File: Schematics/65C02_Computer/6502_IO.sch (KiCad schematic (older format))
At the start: 28 parts, among them J10 LCD Connector, J2 Optional UART Port, J3 USB_B_Micro, J4 USB_B, J5 Power Connector, J6 Mini-DIN-6, J8 VIA2PA, J9 VIA2PB, U10 ATtiny4313-PU, U11 65C22S, U12 65C22S, U5 65C51N, U6 FT230XS, X2 1.8432MHz

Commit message: Added ferrite bead, got rid of DRC errors, other changes
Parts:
- added FB1: Ferrite_Bead_Small, Resistor_THT:R_Axial_DIN0207_L6.3mm_D2.5mm_P7.62mm_Horizontal, symbol Device:Ferrite_Bead_Small
- J4: symbol Connector:USB_B -> 6502:USB_B
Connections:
- net +5V: now also FB1.1; no longer J3.1 (VBUS), J4.1 (VBUS)
- new net: FB1.2, J3.1 (VBUS), J4.1 (VBUS)
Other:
- moved on the sheet: J4
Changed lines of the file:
@@
 	2950 6800 2850 6800
 $Comp
-L Connector:USB_B J4
+L 6502:USB_B J4
 U 1 1 5E5D8CF6
-P 3950 6800
-F 0 "J4" H 4007 7267 50  0000 C CNN
-F 1 "USB_B" H 4007 7176 50  0000 C CNN
-F 2 "Connector_USB:USB_B_OST_USB-B1HSxx_Horizontal" H 4100 6750 50  0001 C CNN
-F 3 " ~" H 4100 6750 50  0001 C CNN
-	1    3950 6800
+P 4200 6800
+F 0 "J4" H 4257 7267 50  0000 C CNN
+F 1 "USB_B" H 4257 7176 50  0000 C CNN
+F 2 "Connector_USB:USB_B_OST_USB-B1HSxx_Horizontal" H 4350 6750 50  0001 C CNN
+F 3 " ~" H 4350 6750 50  0001 C CNN
+	1    4200 6800
 	1    0    0    -1
 $EndComp
-Text GLabel 3950 7300 3    50   Input ~ 0
+Text GLabel 4200 7300 3    50   Input ~ 0
 GND
-Text GLabel 4350 6600 2    50   Input ~ 0
-+5V
-Text GLabel 4350 6800 2    50   BiDi ~ 0
+Text GLabel 4600 6800 2    50   BiDi ~ 0
 PUSBD+
-Text GLabel 4350 6900 2    50   BiDi ~ 0
+Text GLabel 4600 6900 2    50   BiDi ~ 0
 PUSBD-
-NoConn ~ 3850 7200
+NoConn ~ 4100 7200
 Wire Wire Line
-	3950 7300 3950 7200
+	4200 7300 4200 7200
 Wire Wire Line
-	4250 6900 4350 6900
+	4500 6900 4600 6900
 Wire Wire Line
-	4250 6800 4350 6800
+	4500 6800 4600 6800
 Wire Wire Line
-	4250 6600 4350 6600
+	4500 6600 4600 6600
 Wire Wire Line
 	4000 2100 4000 2200
@@
 	2000 1450 1550 1450
 Connection ~ 1550 1450
-Text GLabel 5700 6600 2    50   Input ~ 0
+Text GLabel 6550 6600 2    50   Input ~ 0
 +5V
 Text GLabel 5300 7300 3    50   Input ~ 0
@@
 Text GLabel 1450 1450 0    50   BiDi ~ 0
 PUSBD-
+$Comp
+L Device:Ferrite_Bead_Small FB1
+U 1 1 5E6E4D6F
+P 6100 6600
+F 0 "FB1" V 5863 6600 50  0000 C CNN
+F 1 "Ferrite_Bead_Small" V 5954 6600 50  0000 C CNN
+F 2 "Resistor_THT:R_Axial_DIN0207_L6.3mm_D2.5mm_P7.62mm_Horizontal" V 6030 6600 50  0001 C CNN
+F 3 "~" H 6100 6600 50  0001 C CNN
+	1    6100 6600
+	0    1    1    0
+$EndComp
+Wire Wire Line
+	6200 6600 6400 6600
+Wire Wire Line
+	4600 6600 4600 6250
+Wire Wire Line
+	4600 6250 5700 6250
+Wire Wire Line
+	5700 6250 5700 6600
+Wire Wire Line
+	5700 6600 6000 6600
+Connection ~ 5700 6600
 Wire Bus Line
 	5500 3000 5500 3400
@@
 Wire Bus Line
 	750  5850 750  7400
+$Comp
+L power:PWR_FLAG #FLG0101
+U 1 1 5E78C1CB
+P 6400 6600
+F 0 "#FLG0101" H 6400 6675 50  0001 C CNN
+F 1 "PWR_FLAG" H 6400 6773 50  0000 C CNN
+F 2 "" H 6400 6600 50  0001 C CNN
+F 3 "~" H 6400 6600 50  0001 C CNN
+	1    6400 6600
+	-1   0    0    1
+$EndComp
+Connection ~ 6400 6600
+Wire Wire Line
+	6400 6600 6550 6600
 $EndSCHEMATC

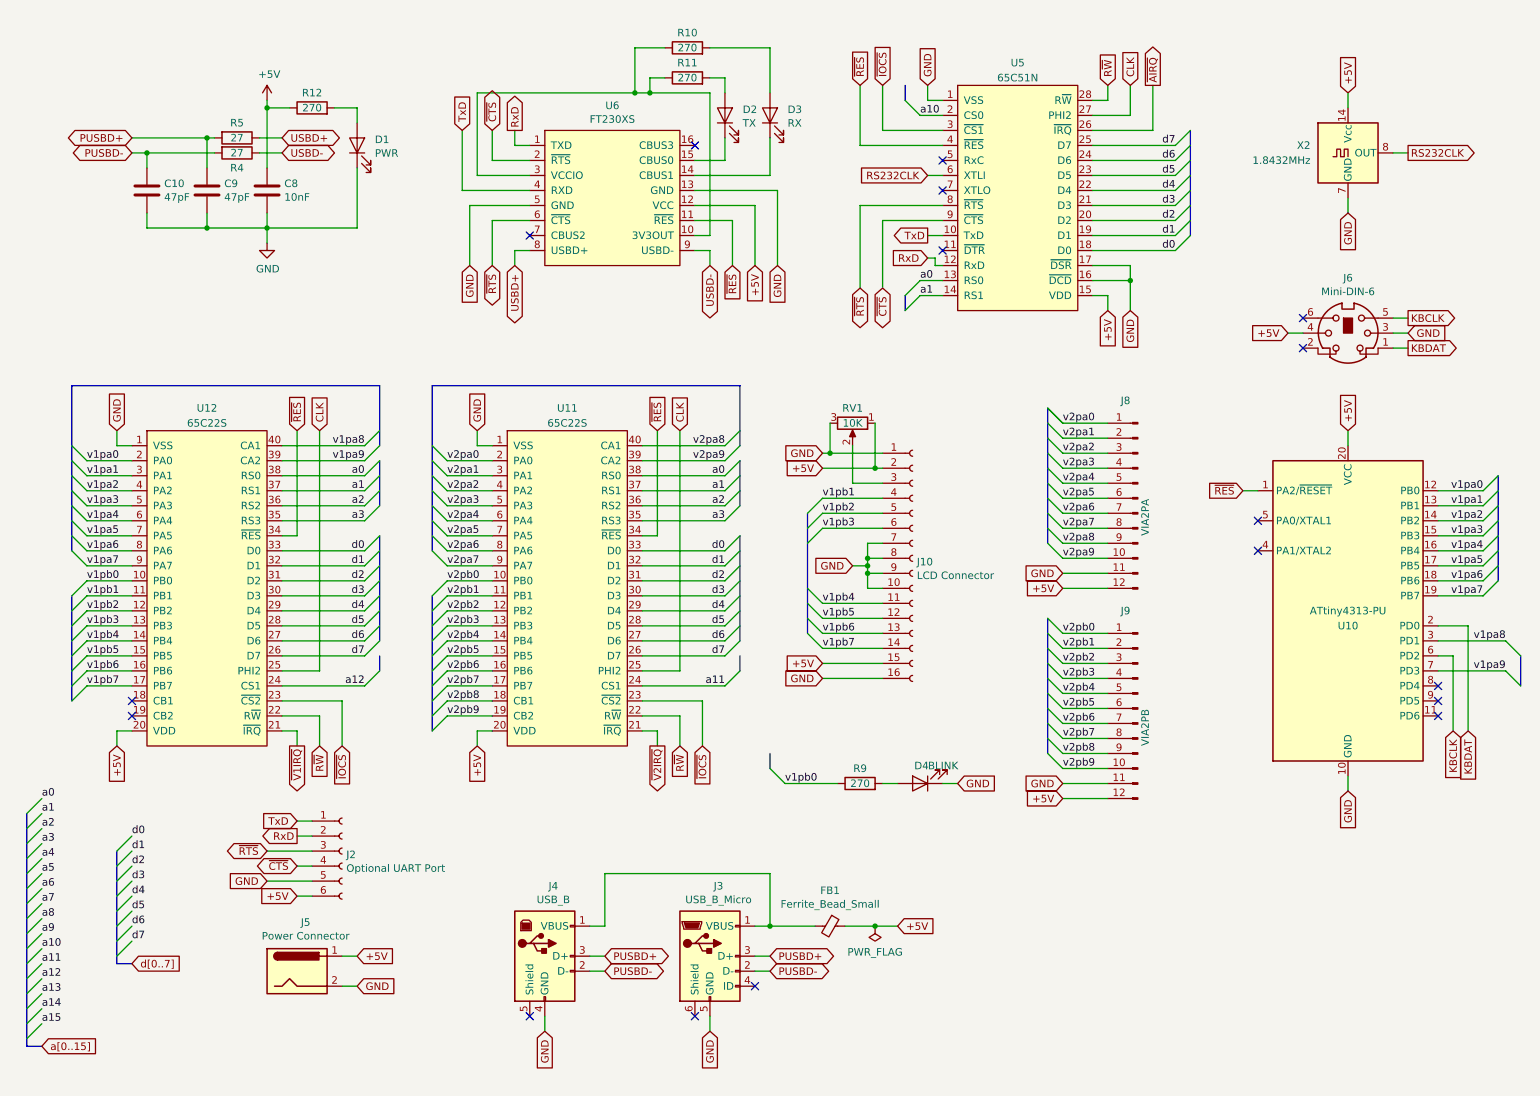
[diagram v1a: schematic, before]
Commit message: Added AVR ISP interface
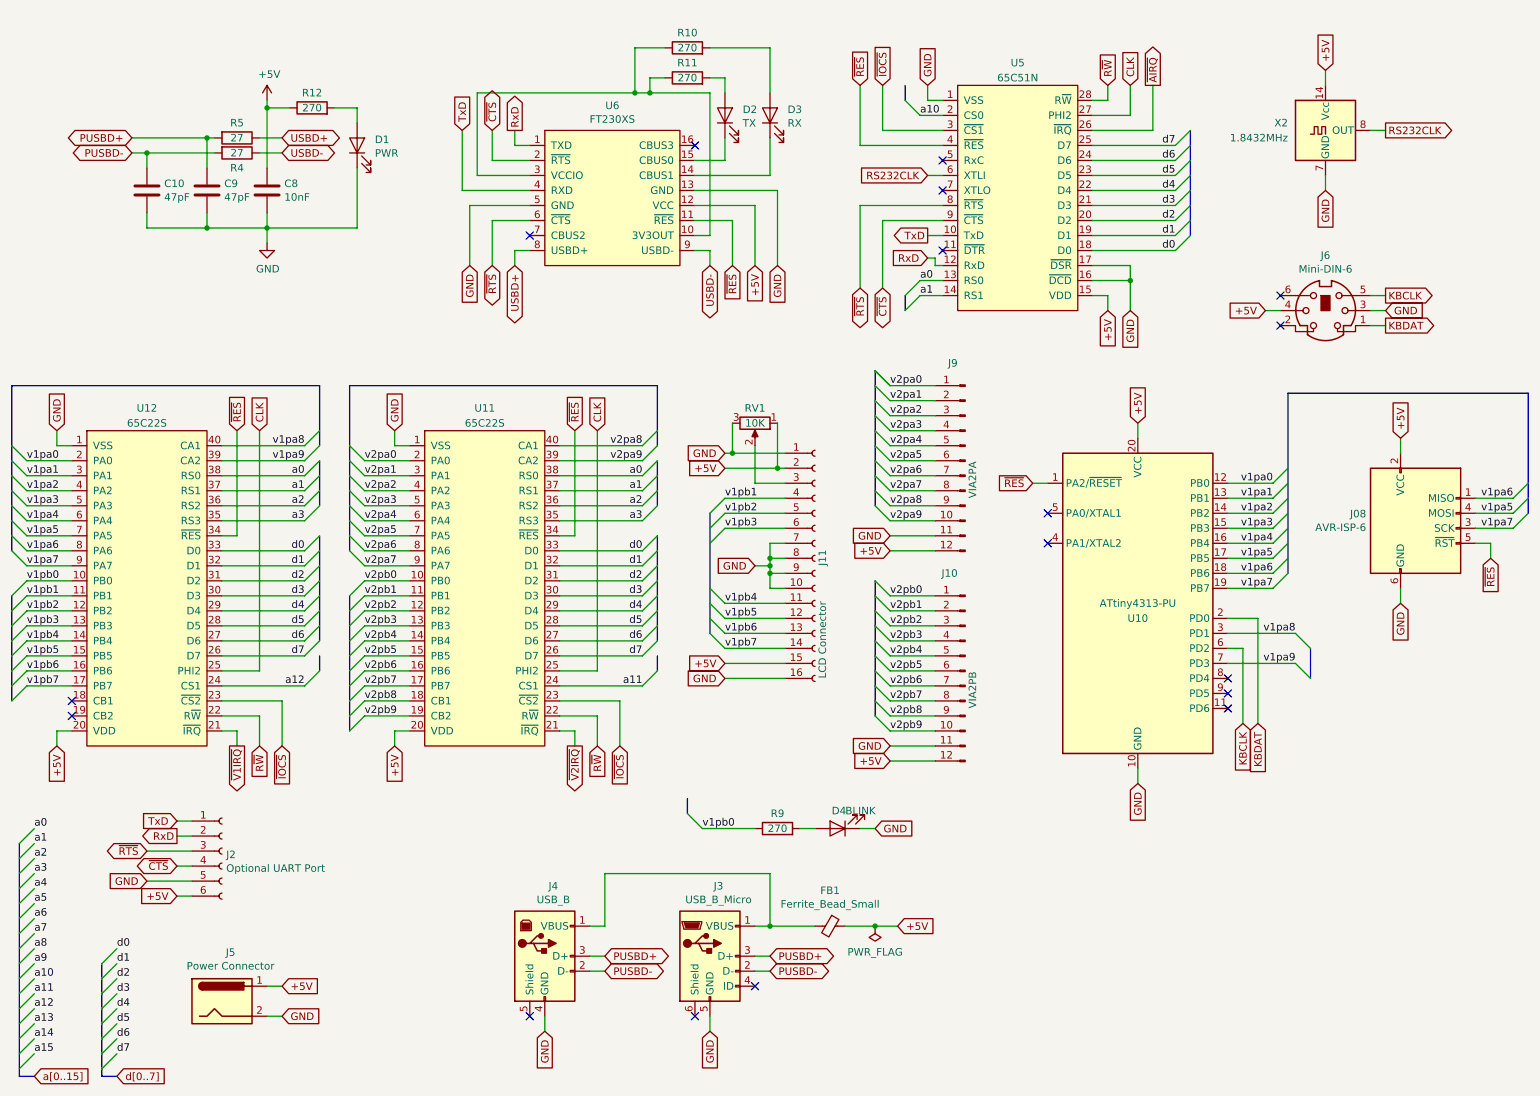
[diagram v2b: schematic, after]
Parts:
- added J08: AVR-ISP-6, Connector_IDC:IDC-Header_2x03_P2.54mm_Vertical, symbol Connector:AVR-ISP-6
- renumbered J9 to J10, J10 to J11, J8 to J9
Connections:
- net +5V: now also J08.2 (VCC)
- net GND: now also J08.6 (GND)
- net v1pa5: now also J08.4 (MOSI)
- net v1pa6: now also J08.1 (MISO)
- net v1pa7: now also J08.3 (SCK)
- net ~RES: now also J08.5 (~RST)
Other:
- moved on the sheet: D4, J10, J11, J2, J5, J6, J9, R9, RV1, U10, U11, U12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

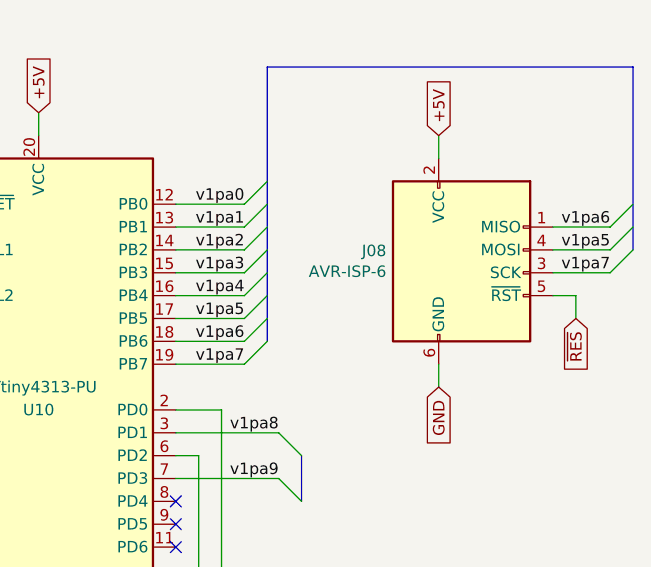
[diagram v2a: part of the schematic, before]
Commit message: Changed AVR ISP port to 10-pin
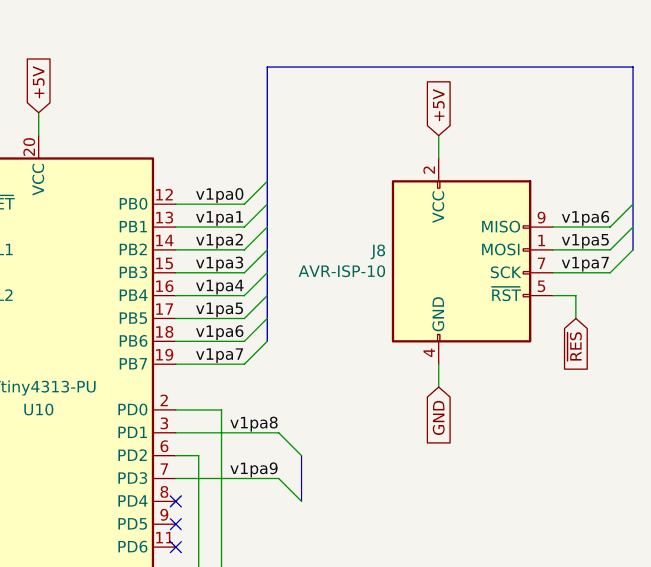
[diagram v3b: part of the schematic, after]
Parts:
- removed J08: AVR-ISP-6, Connector_IDC:IDC-Header_2x03_P2.54mm_Vertical, symbol Connector:AVR-ISP-6
- added J8: AVR-ISP-10, Connector_IDC:IDC-Header_2x05_P2.54mm_Vertical, symbol Connector:AVR-ISP-10
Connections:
- net +5V: now also J8.2 (VCC)
- net GND: now also J8.10 (GND), J8.4 (GND), J8.6 (GND), J8.8 (GND)
- net v1pa5: now also J8.1 (MOSI)
- net v1pa6: now also J8.9 (MISO)
- net v1pa7: now also J8.7 (SCK)
- net ~RES: now also J8.5 (~RST)
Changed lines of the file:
@@
 Wire Wire Line
 	6400 6600 6550 6600
-$Comp
-L Connector:AVR-ISP-6 J08
-U 1 1 5E54741D
-P 10000 3950
-F 0 "J08" H 9671 4046 50  0000 R CNN
-F 1 "AVR-ISP-6" H 9671 3955 50  0000 R CNN
-F 2 "Connector_IDC:IDC-Header_2x03_P2.54mm_Vertical" V 9750 4000 50  0001 C CNN
-F 3 " ~" H 8725 3400 50  0001 C CNN
-	1    10000 3950
-	1    0    0    -1
-$EndComp
 Text GLabel 9900 3350 1    50   Input ~ 0
 +5V
@@
 	10400 3950 10650 3950
 Wire Wire Line
-	10400 3850 10650 3850
-Wire Wire Line
 	10400 3750 10650 3750
 Entry Wire Line
@@
 	10750 3050 9150 3050
 Wire Bus Line
-	4950 3000 4950 3400
-Wire Bus Line
-	2700 3000 2700 3400
-Wire Bus Line
-	4950 3500 4950 3800
-Wire Bus Line
-	2700 3500 2700 3800
-Wire Bus Line
 	10750 3050 10750 3850
 Wire Bus Line
-	8500 1300 8500 2000
+	1250 6850 1250 7600
 Wire Bus Line
-	4950 4000 4950 4700
-Wire Bus Line
-	650  4400 650  5100
-Wire Bus Line
-	2700 4000 2700 4700
-Wire Bus Line
-	5300 3850 5300 4650
+	700  6050 700  7600
 Wire Bus Line
 	9150 3050 9150 4250
-Wire Bus Line
-	1250 6850 1250 7600
 Wire Bus Line
 	6400 4300 6400 5200
@@
 	6400 2900 6400 3800
 Wire Bus Line
+	5300 3850 5300 4650
+Wire Bus Line
+	4950 3000 4950 3400
+Wire Bus Line
+	2700 3000 2700 3400
+Wire Bus Line
+	2700 4000 2700 4700
+Wire Bus Line
+	2700 3500 2700 3800
+Wire Bus Line
 	2900 4400 2900 5300
 Wire Bus Line
 	2900 3000 2900 4100
 Wire Bus Line
+	650  4400 650  5100
+Wire Bus Line
 	650  3000 650  4100
 Wire Bus Line
-	700  6050 700  7600
+	4950 4000 4950 4700
+Wire Bus Line
+	4950 3500 4950 3800
+Wire Bus Line
+	8500 1300 8500 2000
+Wire Wire Line
+	10400 3850 10650 3850
+$Comp
+L Connector:AVR-ISP-10 J8
+U 1 1 5E902E5F
+P 10000 3950
+F 0 "J8" H 9670 4046 50  0000 R CNN
+F 1 "AVR-ISP-10" H 9670 3955 50  0000 R CNN
+F 2 "Connector_IDC:IDC-Header_2x05_P2.54mm_Vertical" V 9750 4000 50  0001 C CNN
+F 3 " ~" H 8725 3400 50  0001 C CNN
+	1    10000 3950
+	1    0    0    -1
+$EndComp
 $EndSCHEMATC

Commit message: Added one more Cap for stable power
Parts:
- J8: footprint Connector_IDC:IDC-Header_2x05_P2.54mm_Vertical -> Connector_PinHeader_2.54mm:PinHeader_2x03_P2.54mm_Vertical; symbol Connector:AVR-ISP-10 -> Connector:AVR-ISP-6
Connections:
- net GND: no longer J8.10 (GND), J8.4 (GND), J8.8 (GND)
- net v1pa5: now also J8.4 (MOSI); no longer J8.1 (MOSI)
- net v1pa6: now also J8.1 (MISO); no longer J8.9 (MISO)
- net v1pa7: now also J8.3 (SCK); no longer J8.7 (SCK)
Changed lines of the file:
@@
 Wire Bus Line
 	10750 3050 9150 3050
+Wire Wire Line
+	10400 3850 10650 3850
+$Comp
+L Connector:AVR-ISP-6 J8
+U 1 1 5E902E5F
+P 10000 3950
+F 0 "J8" H 9670 4046 50  0000 R CNN
+F 1 "AVR-ISP-10" H 9670 3955 50  0000 R CNN
+F 2 "Connector_PinHeader_2.54mm:PinHeader_2x03_P2.54mm_Vertical" V 9750 4000 50  0001 C CNN
+F 3 " ~" H 8725 3400 50  0001 C CNN
+	1    10000 3950
+	1    0    0    -1
+$EndComp
+Wire Bus Line
+	4950 3000 4950 3400
+Wire Bus Line
+	2700 3000 2700 3400
+Wire Bus Line
+	4950 3500 4950 3800
+Wire Bus Line
+	2700 3500 2700 3800
 Wire Bus Line
 	10750 3050 10750 3850
 Wire Bus Line
+	8500 1300 8500 2000
+Wire Bus Line
+	4950 4000 4950 4700
+Wire Bus Line
+	650  4400 650  5100
+Wire Bus Line
+	2700 4000 2700 4700
+Wire Bus Line
+	5300 3850 5300 4650
+Wire Bus Line
 	1250 6850 1250 7600
-Wire Bus Line
-	700  6050 700  7600
 Wire Bus Line
 	9150 3050 9150 4250
@@
 	6400 2900 6400 3800
 Wire Bus Line
-	5300 3850 5300 4650
-Wire Bus Line
-	4950 3000 4950 3400
-Wire Bus Line
-	2700 3000 2700 3400
-Wire Bus Line
-	2700 4000 2700 4700
-Wire Bus Line
-	2700 3500 2700 3800
-Wire Bus Line
 	2900 4400 2900 5300
 Wire Bus Line
 	2900 3000 2900 4100
 Wire Bus Line
-	650  4400 650  5100
-Wire Bus Line
 	650  3000 650  4100
 Wire Bus Line
-	4950 4000 4950 4700
-Wire Bus Line
-	4950 3500 4950 3800
-Wire Bus Line
-	8500 1300 8500 2000
-Wire Wire Line
-	10400 3850 10650 3850
-$Comp
-L Connector:AVR-ISP-10 J8
-U 1 1 5E902E5F
-P 10000 3950
-F 0 "J8" H 9670 4046 50  0000 R CNN
-F 1 "AVR-ISP-10" H 9670 3955 50  0000 R CNN
-F 2 "Connector_IDC:IDC-Header_2x05_P2.54mm_Vertical" V 9750 4000 50  0001 C CNN
-F 3 " ~" H 8725 3400 50  0001 C CNN
-	1    10000 3950
-	1    0    0    -1
-$EndComp
+	700  6050 700  7600
 $EndSCHEMATC

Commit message: PCB RC9 - replaced potentiometers
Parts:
- RV1: footprint Potentiometer_THT:Potentiometer_Runtron_RM-065_Vertical -> Potentiometer_THT:Potentiometer_Piher_PT-10-V10_Vertical
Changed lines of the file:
@@
 F 0 "RV1" V 5500 3250 50  0000 C CNN
 F 1 "10K" V 5600 3250 50  0000 C CNN
-F 2 "Potentiometer_THT:Potentiometer_Runtron_RM-065_Vertical" H 5600 3250 50  0001 C CNN
+F 2 "Potentiometer_THT:Potentiometer_Piher_PT-10-V10_Vertical" H 5600 3250 50  0001 C CNN
 F 3 "~" H 5600 3250 50  0001 C CNN
 	1    5600 3250
